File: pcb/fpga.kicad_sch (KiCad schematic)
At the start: 20 parts, among them J12 MEM_WR_RD_J, J13 KB, J5 FPGA JTAG, J7 RAM cacheable, J8 ROM cacheable, U2 XC2S100TQ144, Y1 TXC-7C, Y2 GTXO-14T

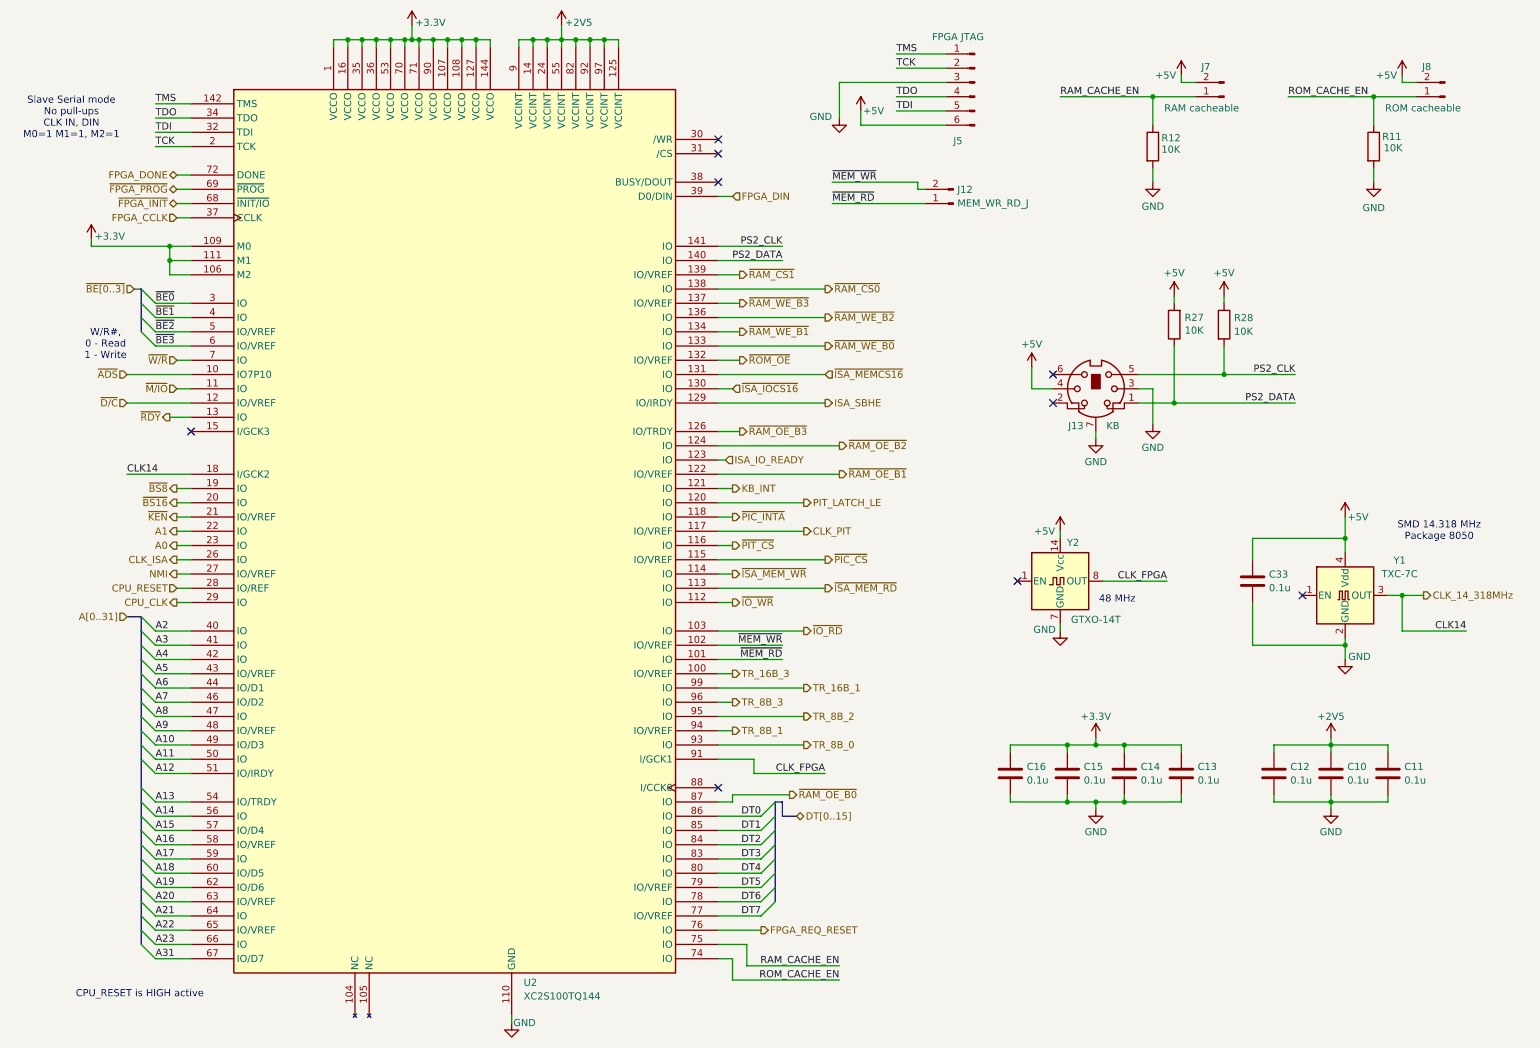
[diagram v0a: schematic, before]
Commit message: fpga diagram aligned and reinforces FPGA decoupling
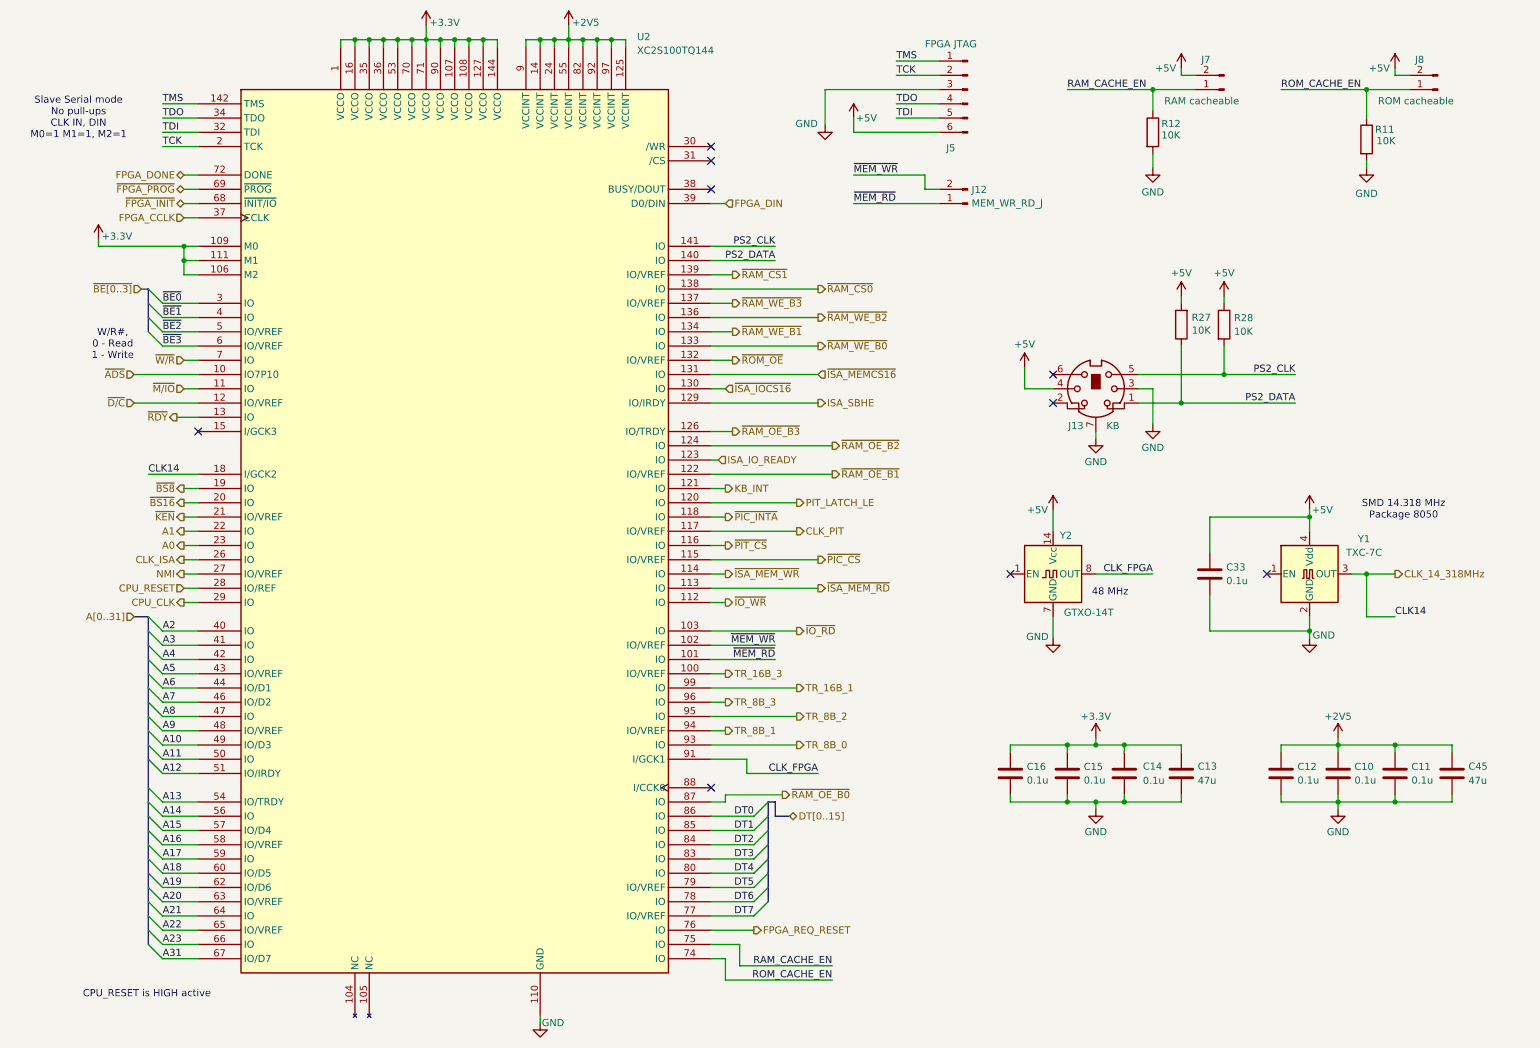
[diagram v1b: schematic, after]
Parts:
- removed C14: 0.1u, Capacitor_SMD:C_0805_2012Metric_Pad1.18x1.45mm_HandSolder, symbol Device:C
- added C13, C45: 47u, Capacitor_SMD:C_1210_3225Metric, symbol Device:C
- renumbered C13 to C14
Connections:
- net +2V5: now also C45.2
- net +3.3V: now also C13.2
- net GND: now also C13.1, C45.1
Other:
- moved on the sheet: C10, C11, C12, C14, C33, J12, J5, J7, J8, R11, R12, R27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

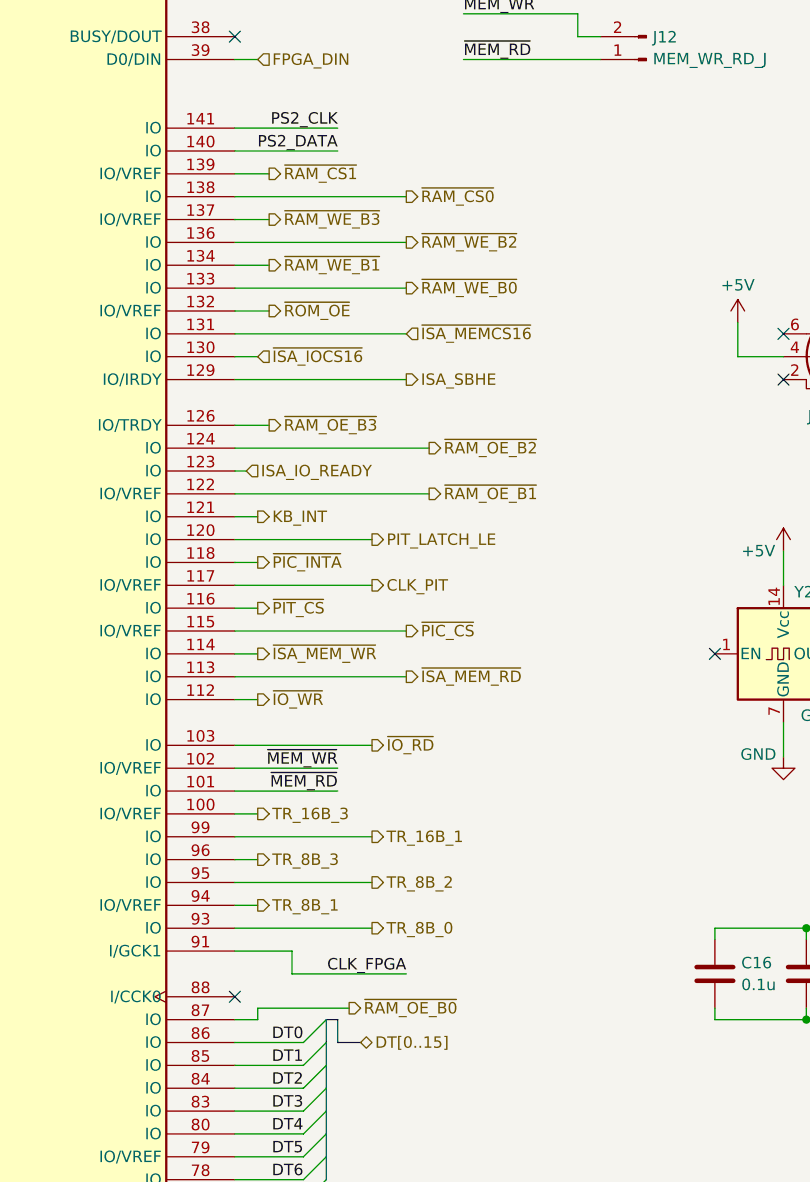
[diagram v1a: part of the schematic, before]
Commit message: swapped P87 RAM_OE_B0/RAM_OE_B<0> and P121 KB_INT/PS2_INTERUPT, 651 VIAs
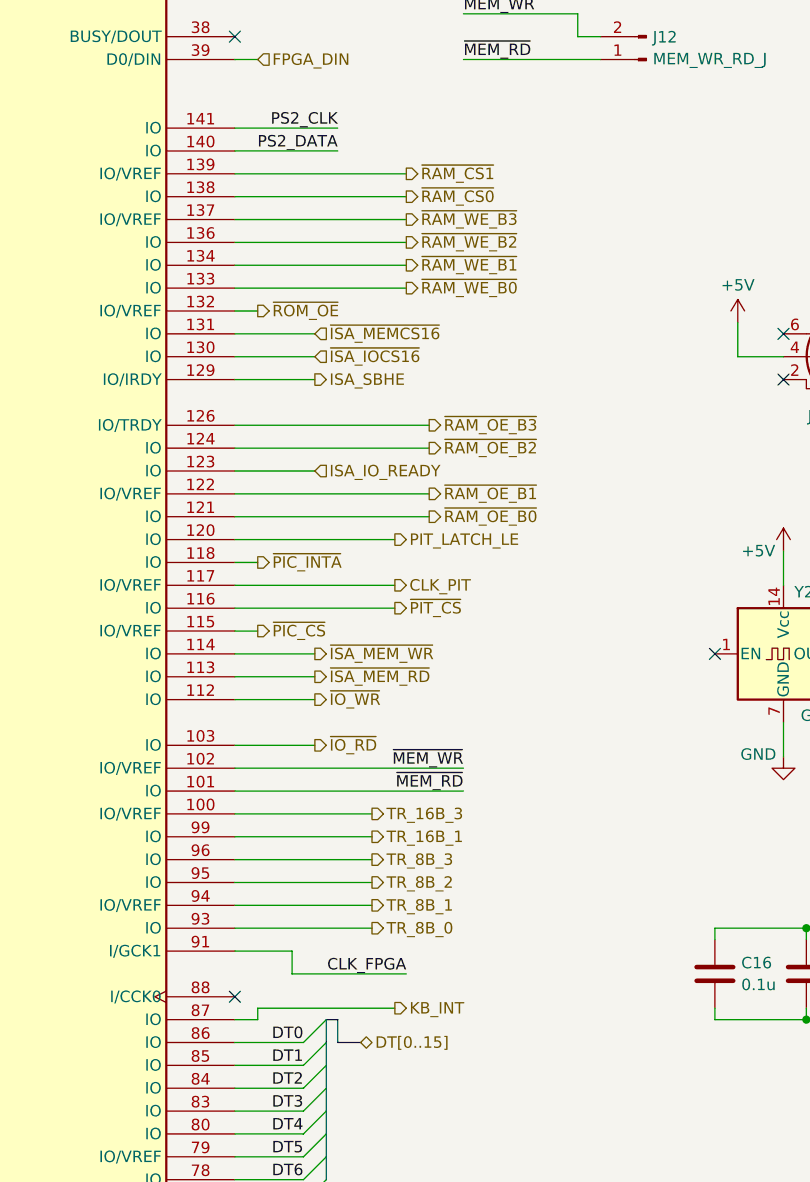
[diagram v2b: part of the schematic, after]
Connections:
- net KB_INT: now also U2.87 (IO); no longer U2.121 (IO)
- net ~{RAM_OE_B0}: now also U2.121 (IO); no longer U2.87 (IO)
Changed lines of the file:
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@@
 	(wire
 		(pts
-			(xy 139.7 83.82) (xy 158.75 83.82)
+			(xy 139.7 83.82) (xy 148.59 83.82)
 		)
 		(stroke
@@
 	(wire
 		(pts
-			(xy 139.7 137.16) (xy 142.24 137.16)
+			(xy 139.7 137.16) (xy 154.94 137.16)
 		)
 		(stroke
@@
 	(wire
 		(pts
-			(xy 139.7 76.2) (xy 143.51 76.2)
+			(xy 139.7 76.2) (xy 142.24 76.2)
 		)
 		(stroke
@@
 	(wire
 		(pts
-			(xy 139.7 71.12) (xy 143.51 71.12)
+			(xy 139.7 71.12) (xy 158.75 71.12)
 		)
 		(stroke
@@
 	(wire
 		(pts
-			(xy 139.7 119.38) (xy 142.24 119.38)
+			(xy 139.7 119.38) (xy 148.59 119.38)
 		)
 		(stroke
@@
 	(wire
 		(pts
-			(xy 139.7 111.76) (xy 158.75 111.76)
+			(xy 139.7 111.76) (xy 142.24 111.76)
 		)
 		(stroke
@@
 	(wire
 		(pts
-			(xy 152.4 153.67) (xy 142.24 153.67)
+			(xy 157.48 153.67) (xy 142.24 153.67)
 		)
 		(stroke
@@
 	(wire
 		(pts
-			(xy 139.7 88.9) (xy 143.51 88.9)
+			(xy 139.7 88.9) (xy 161.29 88.9)
 		)
 		(stroke
@@
 	(wire
 		(pts
-			(xy 139.7 66.04) (xy 143.51 66.04)
+			(xy 139.7 66.04) (xy 158.75 66.04)
 		)
 		(stroke
@@
 	(wire
 		(pts
-			(xy 139.7 124.46) (xy 154.94 124.46)
+			(xy 139.7 124.46) (xy 148.59 124.46)
 		)
 		(stroke
@@
 	(wire
 		(pts
-			(xy 139.7 78.74) (xy 158.75 78.74)
+			(xy 139.7 78.74) (xy 148.59 78.74)
 		)
 		(stroke
@@
 	(wire
 		(pts
-			(xy 139.7 93.98) (xy 140.97 93.98)
+			(xy 139.7 93.98) (xy 148.59 93.98)
 		)
 		(stroke
@@
 	(wire
 		(pts
-			(xy 139.7 114.3) (xy 142.24 114.3)
+			(xy 139.7 114.3) (xy 148.59 114.3)
 		)
 		(stroke
@@
 	(wire
 		(pts
-			(xy 139.7 129.54) (xy 151.13 129.54)
+			(xy 139.7 129.54) (xy 165.1 129.54)
 		)
 		(stroke
@@
 	(wire
 		(pts
-			(xy 139.7 60.96) (xy 143.51 60.96)
+			(xy 139.7 60.96) (xy 158.75 60.96)
 		)
 		(stroke
@@
 	(wire
 		(pts
-			(xy 139.7 99.06) (xy 142.24 99.06)
+			(xy 139.7 99.06) (xy 161.29 99.06)
 		)
 		(stroke
@@
 	(wire
 		(pts
-			(xy 139.7 132.08) (xy 142.24 132.08)
+			(xy 139.7 132.08) (xy 154.94 132.08)
 		)
 		(stroke
@@
 	(wire
 		(pts
-			(xy 139.7 106.68) (xy 154.94 106.68)
+			(xy 139.7 106.68) (xy 157.48 106.68)
 		)
 		(stroke
@@
 	(wire
 		(pts
-			(xy 139.7 81.28) (xy 142.24 81.28)
+			(xy 139.7 81.28) (xy 148.59 81.28)
 		)
 		(stroke
@@
 	(wire
 		(pts
-			(xy 139.7 101.6) (xy 154.94 101.6)
+			(xy 139.7 101.6) (xy 157.48 101.6)
 		)
 		(stroke
@@
 	(wire
 		(pts
-			(xy 139.7 142.24) (xy 142.24 142.24)
+			(xy 139.7 142.24) (xy 154.94 142.24)
 		)
 		(stroke
@@
 	(wire
 		(pts
-			(xy 139.7 109.22) (xy 142.24 109.22)
+			(xy 139.7 127) (xy 165.1 127)
+		)
+		(stroke
+			(width 0)
+			(type default)
+		)
+	)
+	(wire
+		(pts
+			(xy 139.7 109.22) (xy 157.48 109.22)
 		)
 		(stroke
@@
 	(wire
 		(pts
-			(xy 139.7 116.84) (xy 158.75 116.84)
+			(xy 139.7 116.84) (xy 148.59 116.84)
 		)
 		(stroke
@@
 		)
 	)
-	(wire
-		(pts
-			(xy 139.7 127) (xy 151.13 127)
-		)
-		(stroke
-			(width 0)
-			(type default)
-		)
-	)
 	(label "TDO"
 		(at 41.91 33.02 0)
@@
 	)
 	(label "~{MEM_WR}"
-		(at 151.13 127 180)
+		(at 165.1 127 180)
 		(effects
 			(font
@@
 	)
 	(label "~{MEM_RD}"
-		(at 151.13 129.54 180)
+		(at 165.1 129.54 180)
 		(effects
 			(font
@@
 	(hierarchical_label "~{IO_WR}"
 		(shape output)
-		(at 142.24 119.38 0)
+		(at 148.59 119.38 0)
 		(effects
 			(font
@@
 	(hierarchical_label "PIT_LATCH_LE"
 		(shape output)
-		(at 154.94 101.6 0)
+		(at 157.48 101.6 0)
 		(effects
 			(font
@@
 	(hierarchical_label "~{RAM_OE_B3}"
 		(shape output)
-		(at 143.51 88.9 0)
+		(at 161.29 88.9 0)
 		(effects
 			(font
@@
 	(hierarchical_label "~{ISA_MEM_RD}"
 		(shape output)
-		(at 158.75 116.84 0)
-		(effects
-			(font
-				(size 1.27 1.27)
-			)
-			(justify left)
-		)
-	)
-	(hierarchical_label "~{RAM_OE_B0}"
-		(shape output)
-		(at 152.4 153.67 0)
+		(at 148.59 116.84 0)
 		(effects
 			(font
@@
 	(hierarchical_label "~{ISA_IOCS16}"
 		(shape input)
-		(at 142.24 81.28 0)
+		(at 148.59 81.28 0)
 		(effects
 			(font
@@
 	(hierarchical_label "~{PIC_CS}"
 		(shape output)
-		(at 158.75 111.76 0)
+		(at 142.24 111.76 0)
 		(effects
 			(font
@@
 	(hierarchical_label "TR_8B_3"
 		(shape output)
-		(at 142.24 137.16 0)
+		(at 154.94 137.16 0)
 		(effects
 			(font
@@
 	(hierarchical_label "TR_8B_1"
 		(shape output)
-		(at 142.24 142.24 0)
+		(at 154.94 142.24 0)
 		(effects
 			(font
@@
 	(hierarchical_label "~{RAM_WE_B3}"
 		(shape output)
-		(at 143.51 66.04 0)
+		(at 158.75 66.04 0)
 		(effects
 			(font
@@
 	(hierarchical_label "~{PIT_CS}"
 		(shape output)
-		(at 142.24 109.22 0)
+		(at 157.48 109.22 0)
 		(effects
 			(font
@@
 	(hierarchical_label "CLK_PIT"
 		(shape output)
-		(at 154.94 106.68 0)
+		(at 157.48 106.68 0)
 		(effects
 			(font
@@
 		)
 	)
+	(hierarchical_label "~{RAM_OE_B0}"
+		(shape output)
+		(at 161.29 99.06 0)
+		(effects
+			(font
+				(size 1.27 1.27)
+			)
+			(justify left)
+		)
+	)
 	(hierarchical_label "~{RAM_CS0}"
 		(shape output)
@@
 		)
 	)
+	(hierarchical_label "KB_INT"
+		(shape output)
+		(at 157.48 153.67 0)
+		(effects
+			(font
+				(size 1.27 1.27)
+			)
+			(justify left)
+		)
+	)
 	(hierarchical_label "ISA_IO_READY"
 		(shape input)
-		(at 140.97 93.98 0)
+		(at 148.59 93.98 0)
 		(effects
 			(font
@@
 	(hierarchical_label "~{IO_RD}"
 		(shape output)
-		(at 154.94 124.46 0)
+		(at 148.59 124.46 0)
 		(effects
 			(font
@@
 	(hierarchical_label "ISA_SBHE"
 		(shape output)
-		(at 158.75 83.82 0)
+		(at 148.59 83.82 0)
 		(effects
 			(font
@@
 	(hierarchical_label "~{ISA_MEMCS16}"
 		(shape input)
-		(at 158.75 78.74 0)
+		(at 148.59 78.74 0)
 		(effects
 			(font
@@
 		)
 	)
-	(hierarchical_label "KB_INT"
-		(shape output)
-		(at 142.24 99.06 0)
-		(effects
-			(font
-				(size 1.27 1.27)
-			)
-			(justify left)
-		)
-	)
 	(hierarchical_label "~{BS16}"
 		(shape output)
@@
 	(hierarchical_label "~{RAM_WE_B1}"
 		(shape output)
-		(at 143.51 71.12 0)
+		(at 158.75 71.12 0)
 		(effects
 			(font
@@
 	(hierarchical_label "~{ROM_OE}"
 		(shape output)
-		(at 143.51 76.2 0)
+		(at 142.24 76.2 0)
 		(effects
 			(font
@@
 	(hierarchical_label "~{ISA_MEM_WR}"
 		(shape output)
-		(at 142.24 114.3 0)
+		(at 148.59 114.3 0)
 		(effects
 			(font
@@
 	(hierarchical_label "~{RAM_CS1}"
 		(shape output)
-		(at 143.51 60.96 0)
+		(at 158.75 60.96 0)
 		(effects
 			(font
@@
 	(hierarchical_label "TR_16B_3"
 		(shape output)
-		(at 142.24 132.08 0)
+		(at 154.94 132.08 0)
 		(effects
 			(font

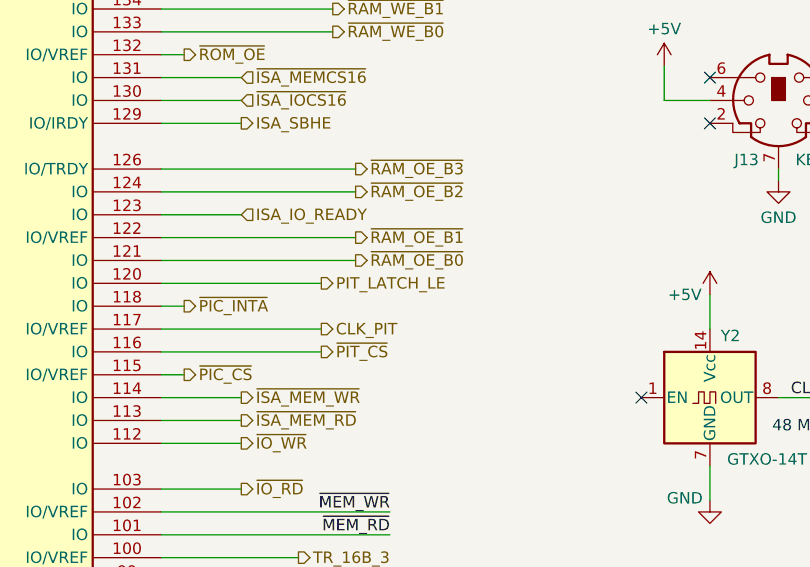
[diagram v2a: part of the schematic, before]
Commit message: updating diagram and pcb to removed U23, driving PIT gate2 directly by PIT_SPK_GATE (former PIT_LATCH_LE), 635 VIAs
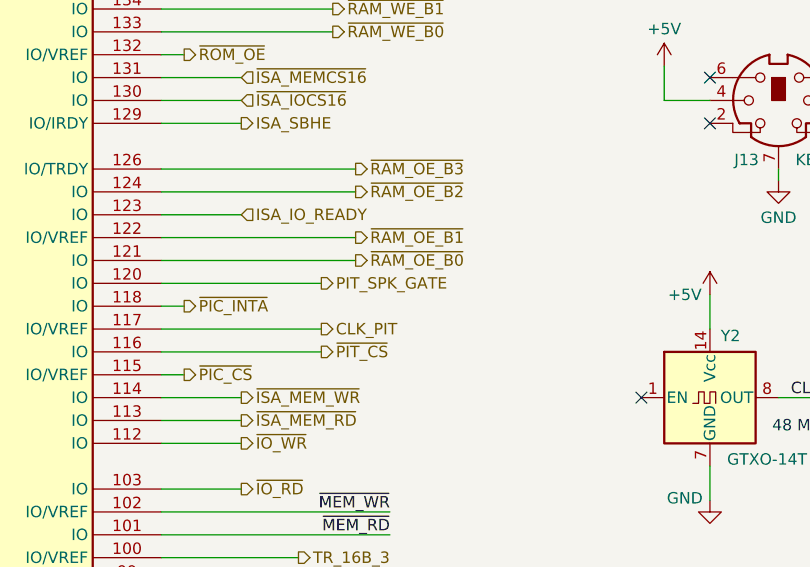
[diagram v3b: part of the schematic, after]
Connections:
- net PIT_LATCH_LE renamed PIT_SPK_GATE
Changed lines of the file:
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@@
 		)
 	)
-	(hierarchical_label "PIT_LATCH_LE"
+	(hierarchical_label "PIT_SPK_GATE"
 		(shape output)
 		(at 157.48 101.6 0)
